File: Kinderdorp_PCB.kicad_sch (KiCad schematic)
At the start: 44 parts, among them Q1 2N7002_C306856, U1 AMS1117-3.3_C347222, U2 ESP32-C3-WROOM-02-N4(4MB)

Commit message: fixed button design error
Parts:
- renumbered BATT+ to BATT+1, BATT- to BATT-1, USB+ to USB+1, USB- to USB-1
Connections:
- net GND: now also BUTTON1.4, BUTTON2.4; no longer BUTTON1.1, BUTTON2.1
- net GPIO4: now also BUTTON1.1; no longer BUTTON1.4
- net GPIO5: now also BUTTON2.1; no longer BUTTON2.4

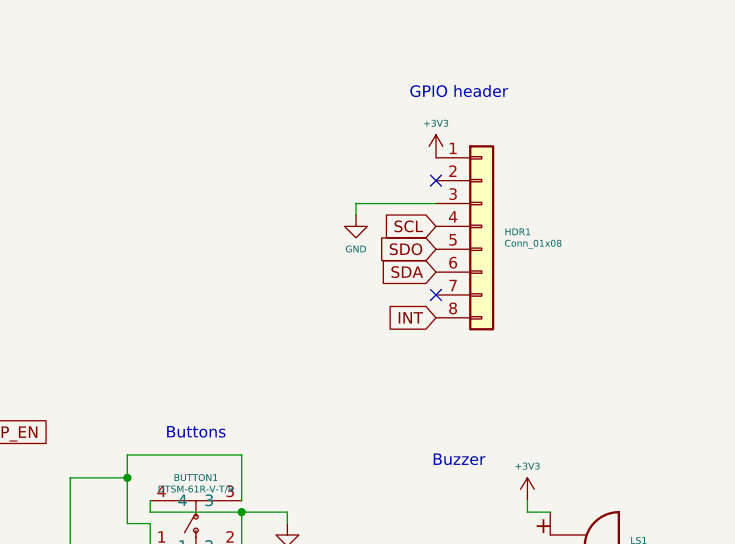
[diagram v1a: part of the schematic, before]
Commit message: added more lighting effects and updated i2c on pcb (header)
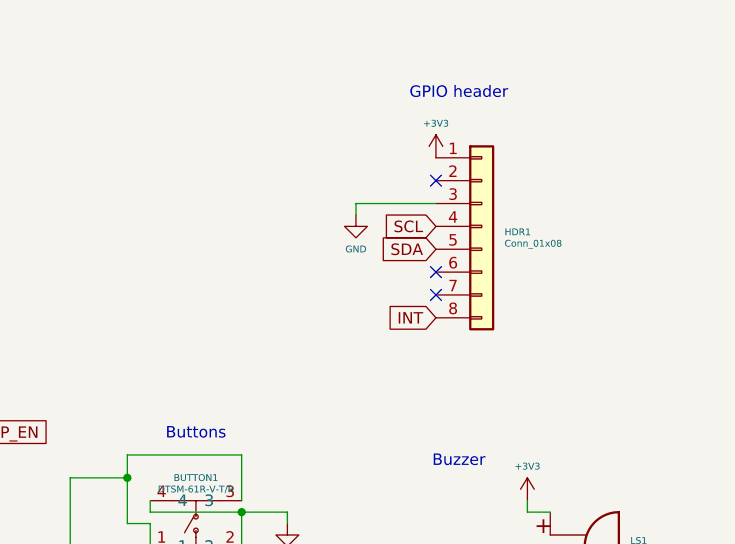
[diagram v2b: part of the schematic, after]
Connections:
- net SDO is gone; now on net GPIO6: HDR1.5 (Pin_5)
- net GPIO6: no longer HDR1.6 (Pin_6)
- no-connect marks 4 -> 5
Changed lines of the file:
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@@
 	(title_block
 		(title "Kinderdorp_PCB")
-		(date "2025-07-27")
-		(rev "V1.0")
+		(date "2025-08-10")
+		(rev "V1.1")
 		(comment 1 "Casper R. Tak")
 	)
@@
 	(no_connect
 		(at 254 34.29)
+	)
+	(no_connect
+		(at 254 44.45)
 	)
 	(no_connect
@@
 		)
 	)
-	(global_label "SDO"
-		(shape input)
-		(at 254 41.91 180)
-		(fields_autoplaced yes)
-		(effects
-			(font
-				(size 1.27 1.27)
-			)
-			(justify right)
-		)
-		(property "Intersheetrefs" "${INTERSHEET_REFS}"
-			(at 247.2048 41.91 0)
-			(effects
-				(font
-					(size 1.27 1.27)
-				)
-				(justify right)
-				(hide yes)
-			)
-		)
-	)
 	(global_label "BATT_V"
 		(shape output)
@@
 		)
 	)
-	(global_label "SDA"
-		(shape input)
-		(at 254 44.45 180)
-		(fields_autoplaced yes)
-		(effects
-			(font
-				(size 1.27 1.27)
-			)
-			(justify right)
-		)
-		(property "Intersheetrefs" "${INTERSHEET_REFS}"
-			(at 247.4467 44.45 0)
-			(effects
-				(font
-					(size 1.27 1.27)
-				)
-				(justify right)
-				(hide yes)
-			)
-		)
-	)
 	(global_label "BUZZ"
 		(shape input)
@@
 			(effects
 				(font
+					(size 1.27 1.27)
+				)
+				(justify right)
+				(hide yes)
+			)
+		)
+	)
+	(global_label "SDA"
+		(shape input)
+		(at 254 41.91 180)
+		(fields_autoplaced yes)
+		(effects
+			(font
+				(size 1.27 1.27)
+			)
+			(justify right)
+		)
+		(property "Intersheetrefs" "${INTERSHEET_REFS}"
+			(at 247.4467 41.91 0)
+			(effects
+				(font

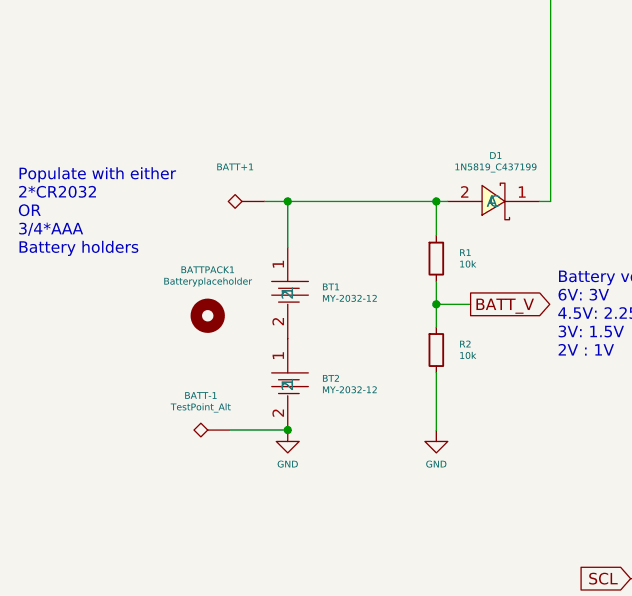
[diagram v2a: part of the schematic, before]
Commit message: updated PCB to V1.1
removed cr2032 (this is not viable with the current draw of the board)
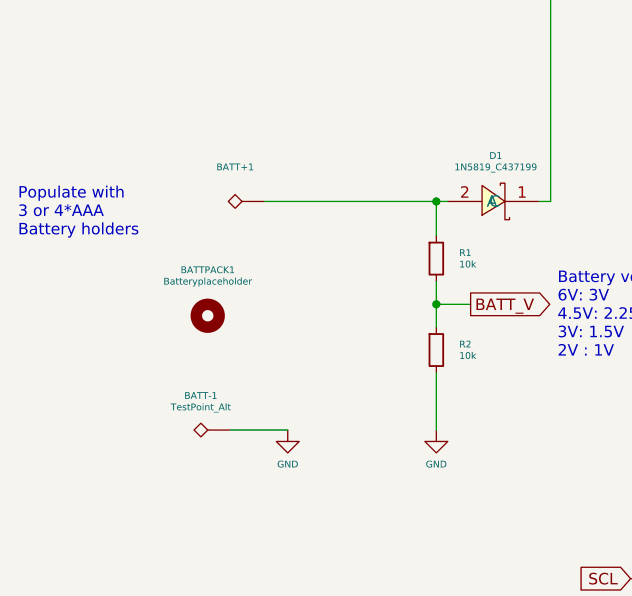
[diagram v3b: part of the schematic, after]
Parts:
- removed BT1, BT2: MY-2032-12, easyeda2kicad:BAT-SMD_MY-2032-12, symbol easyeda2kicad:MY-2032-12
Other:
- note added: "Populate with 3 or 4*AAA Battery holders"
- note removed: "Populate with either 2*CR2032 OR 3/4*AAA Battery holders"
